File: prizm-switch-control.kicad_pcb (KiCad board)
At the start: 2 copper layers, 85 x 56 mm, 45 parts, among them J1 Power Connector, J2 Frontend Connector, P1 RPi-Header, U1 MCP23017_SO, U10 TLP3543, U11 TLP3543, U12 TLP3543, U2 DS3231M, U3 TLP3543, U4 TLP3543, U5 TLP3543, U6 TLP3543, U7 TLP3543, U8 TLP3543, U9 TLP3543

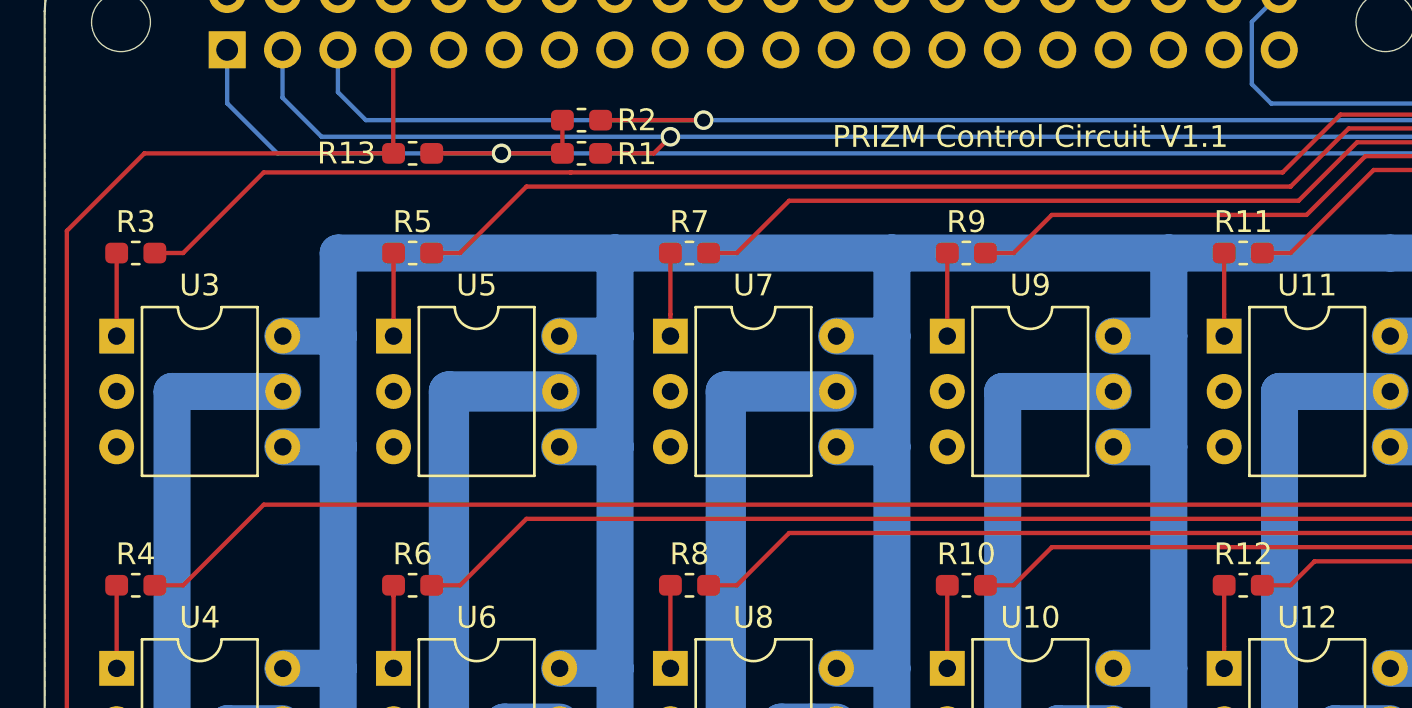
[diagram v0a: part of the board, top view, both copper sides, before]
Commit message: Added MFN, MPN, VN and VPN fields for all symbols
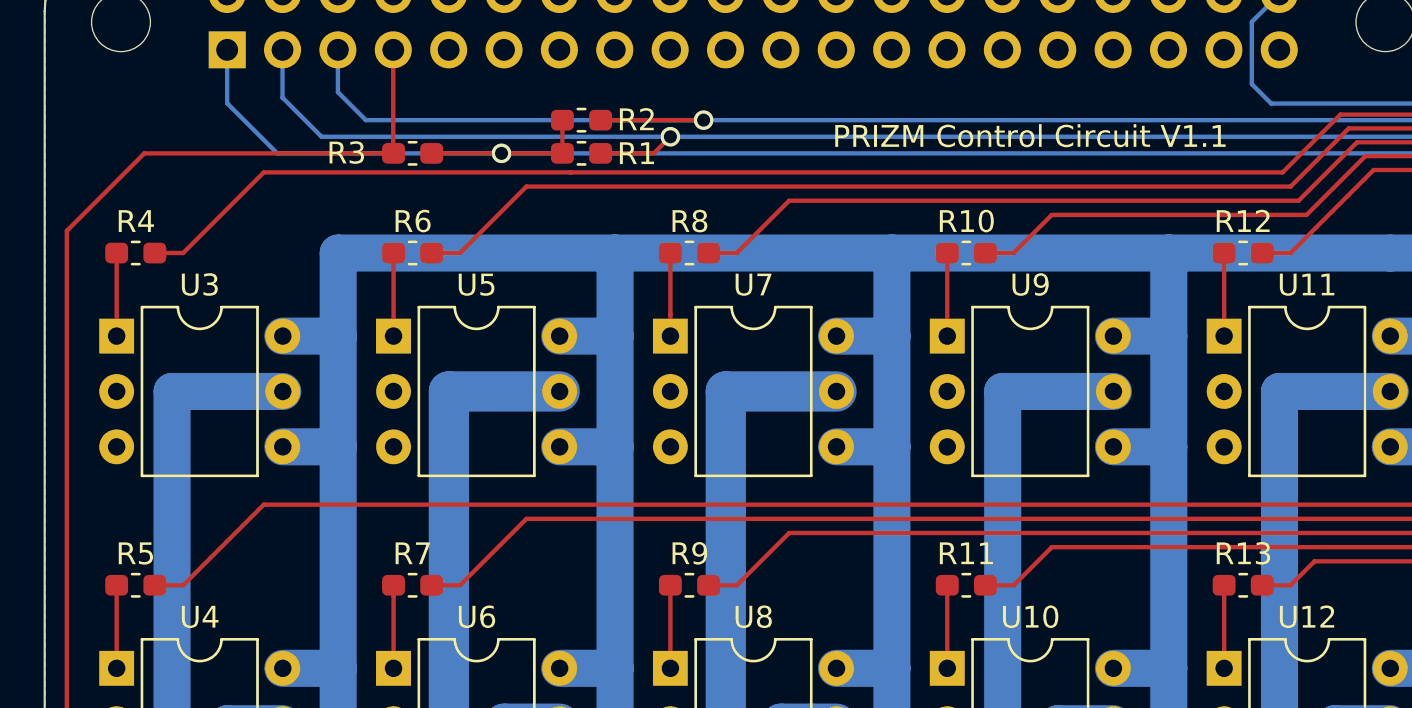
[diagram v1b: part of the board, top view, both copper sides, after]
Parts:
- renumbered R9 to R10, R10 to R11, R11 to R12, R12 to R13, R13 to R3, R3 to R4, R4 to R5, R5 to R6, R6 to R7, R7 to R8, R8 to R9
